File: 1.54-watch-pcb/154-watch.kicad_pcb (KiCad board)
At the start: 4 copper layers, 50.3 x 33 mm, 59 parts, among them J1 CONN_AFC24-S24FIC-00_JUS, J2 Conn_01x06_Female, J3 USB_C_Programming, J4 Jack-DC, J5 Conn_01x02_Male, Q1 Si1308, Q2 BC817, Q3 BC817, Q4 Si2301CDS, SW1 RESET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

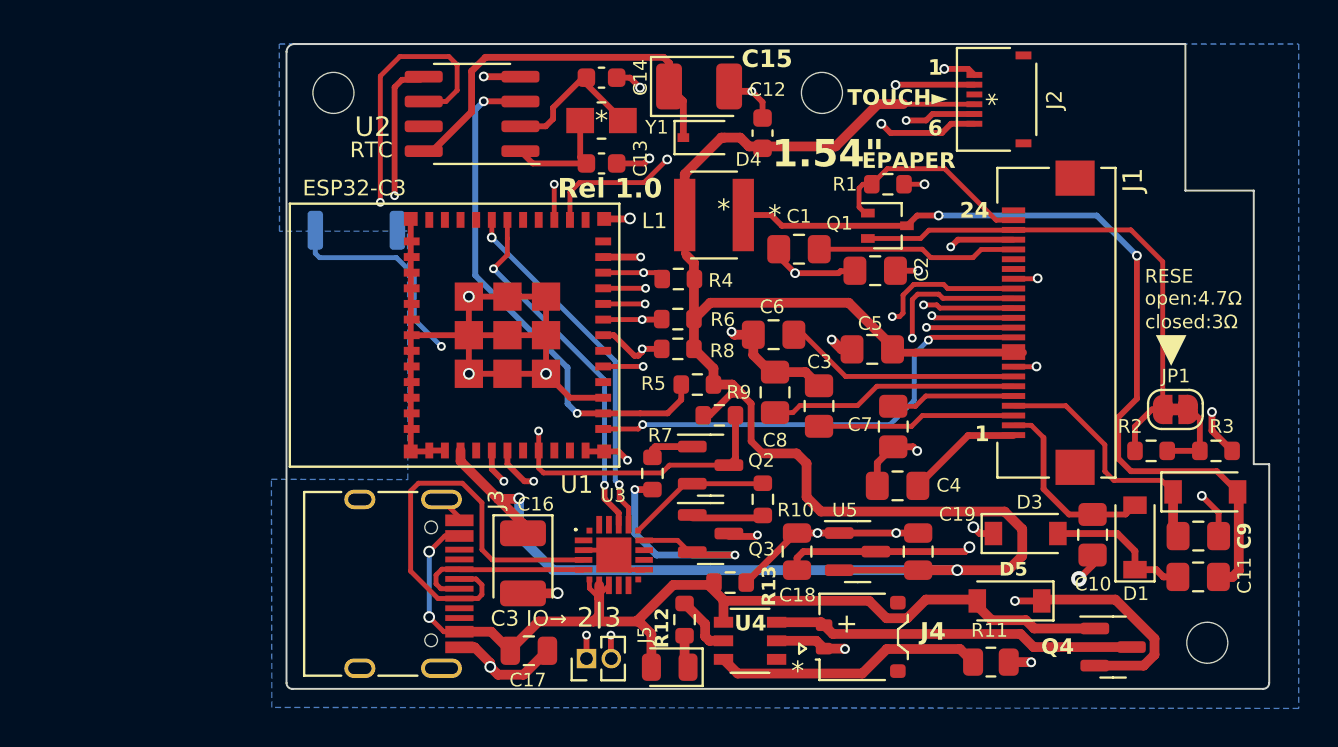
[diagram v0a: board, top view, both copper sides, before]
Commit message: #6 Position well 24 pin FPC
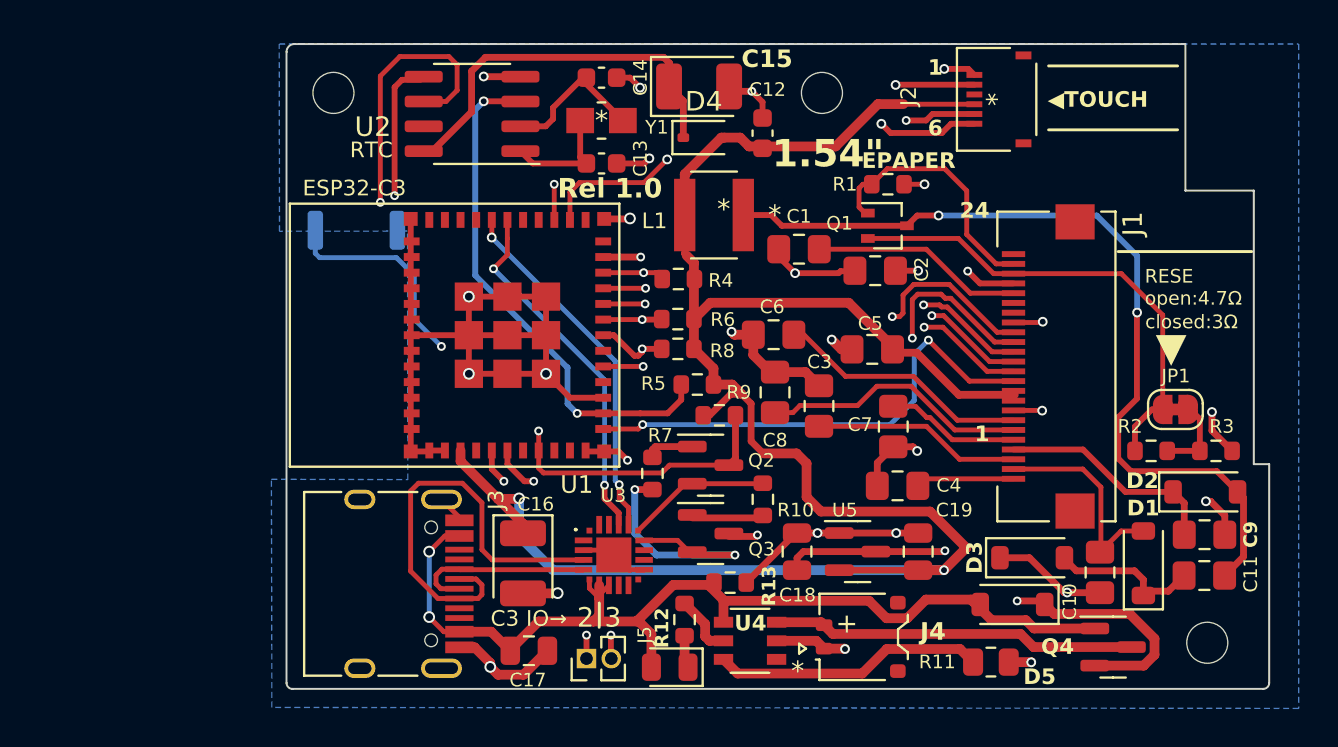
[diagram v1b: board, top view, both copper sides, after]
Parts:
- moved J1 2.24 mm to (111.4, 46.0)
- moved C10 1.96 mm to (113.6, 56.5)
- moved D1 1.39 mm to (115.8, 56.1)
- moved D3 1.28 mm to (110.2, 55.8)
- moved C9 0.33 mm to (119.0, 54.6)
- moved C11 0.33 mm to (119.0, 56.7)
- moved D5 0.23 mm to (109.2, 58.2)
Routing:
- net +3V3: track 112.3 -> 105.6 mm
- net GND: track 103.1 -> 106.7 mm, vias 27 -> 26
- net Net-(Q1-G): track 11.0 -> 13.2 mm
- net Net-(JP1-A): track 26.5 -> 24.6 mm
- net PREVGH: track 13.2 -> 11.5 mm
- net Net-(D1-A): track 9.84 -> 10.9 mm
- net /EPD_CLK: track 21.5 -> 22.4 mm
- net Net-(C8-Pad2): track 12.8 -> 13.7 mm
- net Net-(C6-Pad2): track 12.1 -> 13.1 mm
- net /EPD_RST: track 23.8 -> 24.7 mm
- net /EPD_DC: track 28.0 -> 28.9 mm
- net /EPD_CS: track 28.7 -> 29.7 mm
- net /EPD_BUSY: track 22.9 -> 23.8 mm
- net /VCOM: track 5.96 -> 5.05 mm
- net /EPD_MOSI: track 24.3 -> 25.1 mm
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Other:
- board text added: "◀TOUCH"
- board text removed: "TOUCH►"

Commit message: Add some test points in case UART works incorrectly https://github.com/martinberlin/H-spi-adapters/issues/9
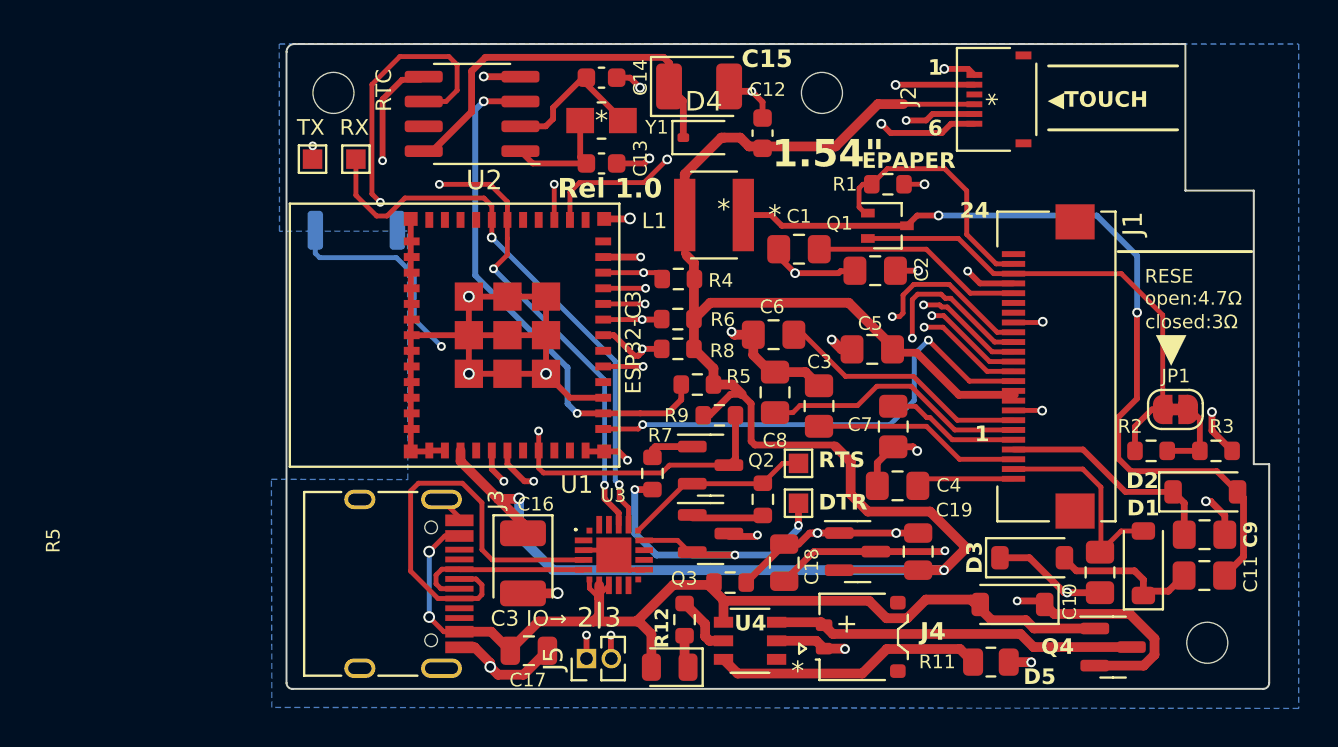
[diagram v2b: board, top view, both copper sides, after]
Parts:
- added TP1: 32Khz, TestPoint:TestPoint_Pad_1.0x1.0mm, F.Cu at (98.2, 51.0)
- added TP2: 32Khz, TestPoint:TestPoint_Pad_1.0x1.0mm, F.Cu at (98.2, 53.0)
- added TP3: 32Khz, TestPoint:TestPoint_Pad_1.0x1.0mm, F.Cu at (73.3, 35.4)
- added TP4: 32Khz, TestPoint:TestPoint_Pad_1.0x1.0mm, F.Cu at (75.5, 35.4)
- J1: value CONN_AFC24-S24FIC-00_JUS -> AFC24-S24FIC-00
- U1: value ESP32-C3-MINI -> ESP32-C3-MINI-1-N4
- U4: value SOT-23-5_TPW -> TP4057-42-SOT26-R
- moved C18 0.87 mm to (97.5, 56.0)
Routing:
- net TX: track 18.6 -> 31.6 mm, vias 2 -> 4
- net RX: track 18.5 -> 29.0 mm
- net /CTS: track 13.7 -> 18.8 mm, vias 2 -> 3
- net BOOTMODE: track 55.4 -> 57.9 mm
- net /RTS: track 7.38 -> 9.65 mm
- net Net-(D5-K): track 25.0 -> 25.6 mm
- net /I2C_SDA: track 49.0 -> 49.5 mm
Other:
- board text added: "DTR"
- board text added: "R5"
- board text added: "RTS"
- board text added: "RX"
- board text added: "TX"

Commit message: 1.54" Rel 1.0 sent to fabrication
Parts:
- moved SW1 0.93 mm to (76.5, 39.0)
- moved D2 0.37 mm to (118.7, 52.3)
- moved C11 0.09 mm to (119.0, 56.8)
- moved C9 0.09 mm to (119.1, 54.6)
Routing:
- net Net-(Q2-C): track 33.7 -> 32.1 mm
- net GND: track 106.9 -> 107.4 mm
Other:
- outline, holes or cut-outs redrawn

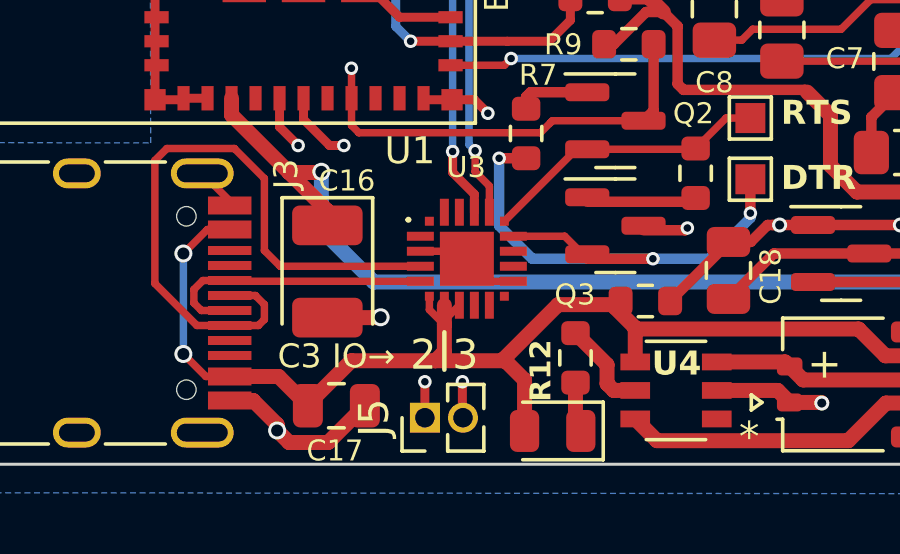
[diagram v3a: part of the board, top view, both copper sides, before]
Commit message: Sharp LCD prod. 1.0 and update to failed watch
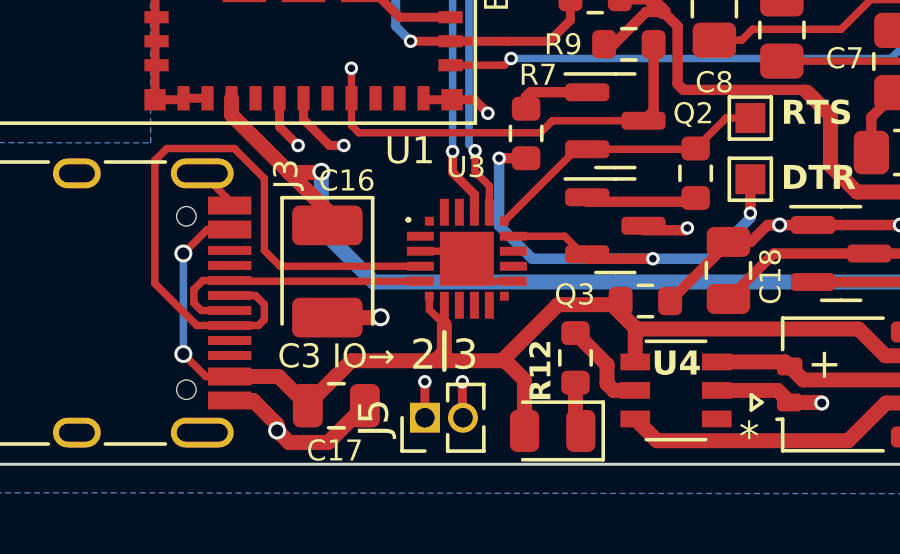
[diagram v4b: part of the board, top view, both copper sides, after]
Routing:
- net VBUS: track 50.9 -> 49.6 mm
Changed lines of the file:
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@@
   (segment (start 89.975 58.995) (end 89.92 59.05) (width 0.5) (layer "F.Cu") (net 3))
   (segment (start 79.3 58.825) (end 80.05 59.575) (width 0.25) (layer "F.Cu") (net 3))
-  (segment (start 88 57.85) (end 88 57.2) (width 0.5) (layer "F.Cu") (net 3))
   (segment (start 80.1 54.675) (end 79.3 55.475) (width 0.25) (layer "F.Cu") (net 3))
   (segment (start 88 58.75) (end 88 57.85) (width 0.5) (layer "F.Cu") (net 3))
@@
   (segment (start 104.721812 57.93) (end 107.03 57.93) (width 0.5) (layer "F.Cu") (net 3))
   (segment (start 87.7 59.05) (end 88 58.75) (width 0.5) (layer "F.Cu") (net 3))
-  (segment (start 88.5 57.2) (end 88 57.7) (width 0.25) (layer "F.Cu") (net 3))
   (segment (start 84.9 59.05) (end 83.45 60.5) (width 0.5) (layer "F.Cu") (net 3))
   (segment (start 82.475 59.575) (end 80.845 59.575) (width 0.5) (layer "F.Cu") (net 3))

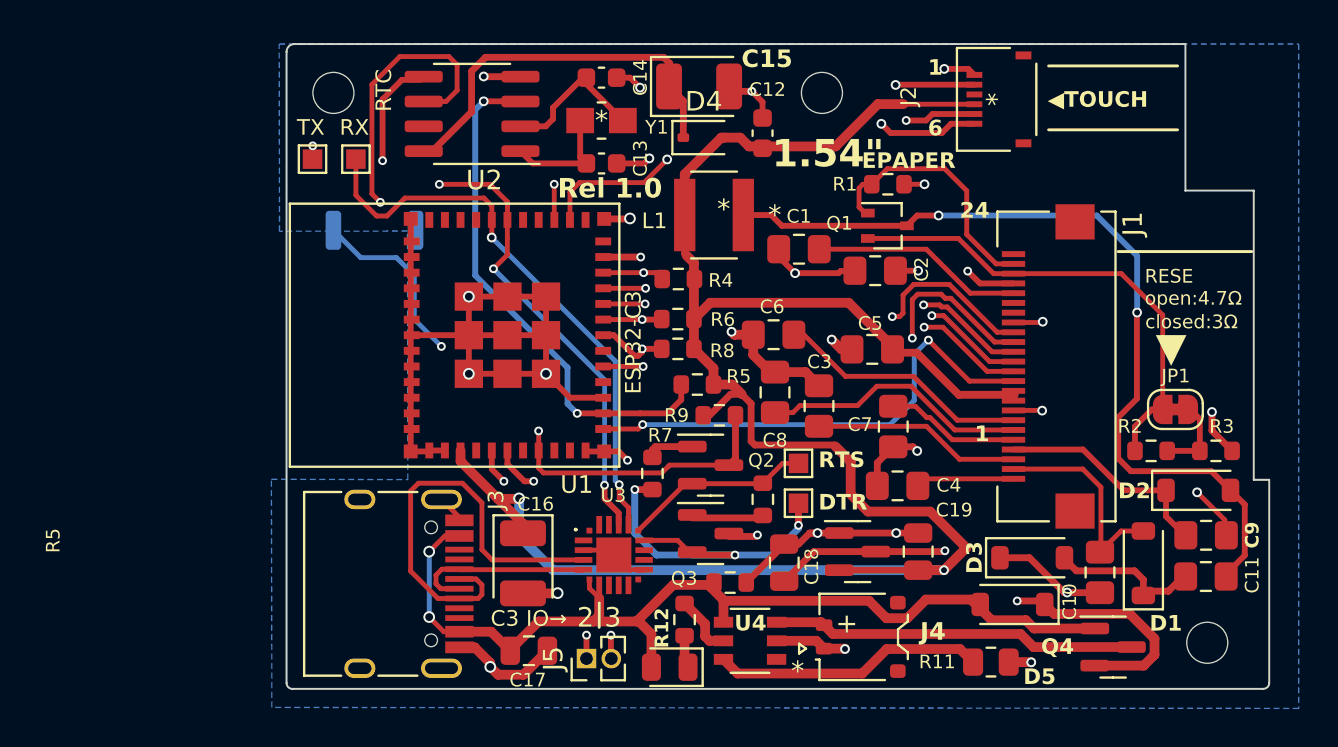
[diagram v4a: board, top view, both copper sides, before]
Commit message: Update UART in 1.54" watch PCB
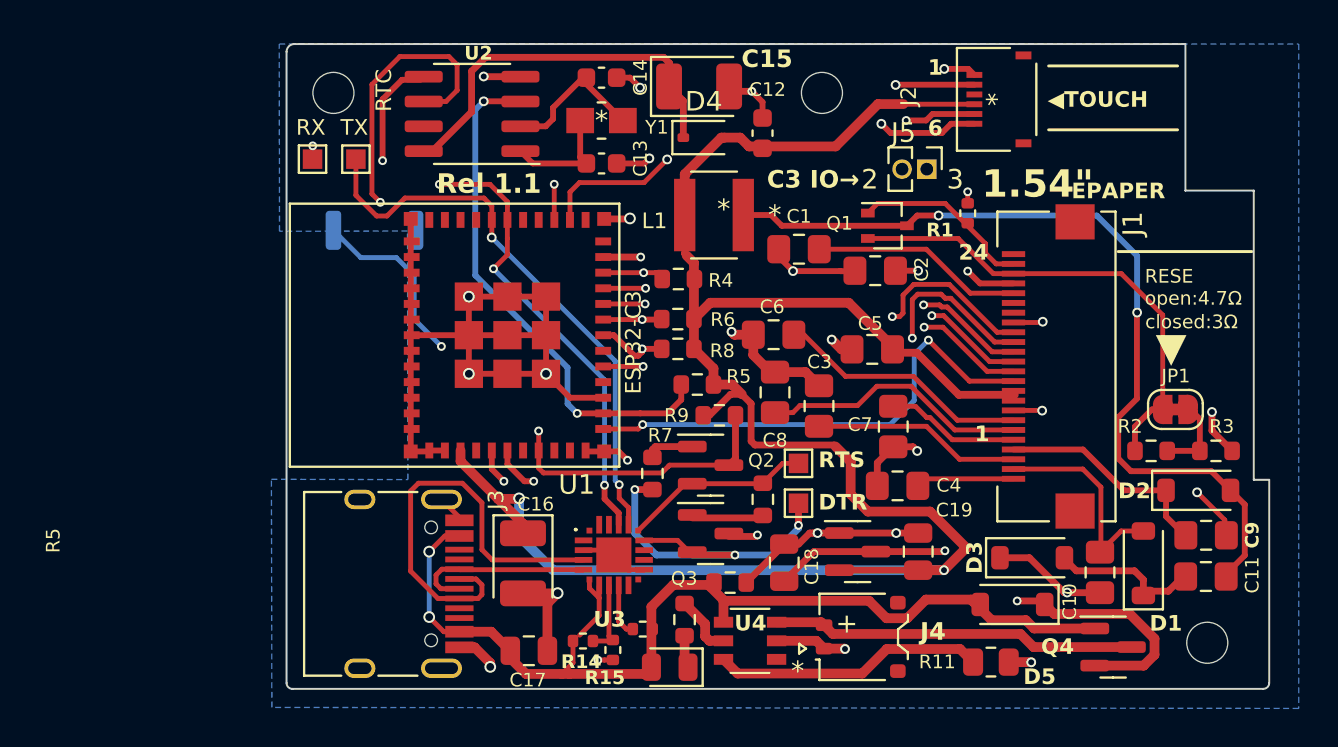
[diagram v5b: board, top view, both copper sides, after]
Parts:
- added R14: 22K, Resistor_SMD:R_0402_1005Metric, F.Cu at (87.2, 60.0)
- added R15: 47K, Resistor_SMD:R_0402_1005Metric, F.Cu at (88.7, 60.5)
- added R16: 10 K, Resistor_SMD:R_0402_1005Metric, F.Cu at (90.2, 59.4)
- R1: footprint Resistor_SMD:R_0603_1608Metric -> Resistor_SMD:R_0402_1005Metric
- moved J5 30.5 mm to (104.8, 35.9), turned to -90 degrees
- moved R1 4.35 mm to (106.9, 38.2), turned to 90 degrees
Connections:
- U3 pad 8: VBUS -> Net-(U3-VBUS)
- U3 pad 9: unconnected-(U3-~{RST}-Pad9) -> Net-(U3-~{RST})
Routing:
- net /IO_2: track 12.7 -> 32.5 mm, vias 2 -> 1
- net /IO_3: track 13.1 -> 28.2 mm, vias 2 -> 1
- net Net-(Q1-G): track 13.2 -> 9.22 mm
- net Net-(U3-VBUS): track 0.00 -> 3.85 mm
- net VBUS: track 49.6 -> 52.9 mm
- net Net-(U3-~{RST}): track 0.00 -> 2.73 mm
- net GND: track 107.4 -> 107.2 mm, vias 26 -> 27
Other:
- board text added: "Rel 1.1"
- board text removed: "Rel 1.0"

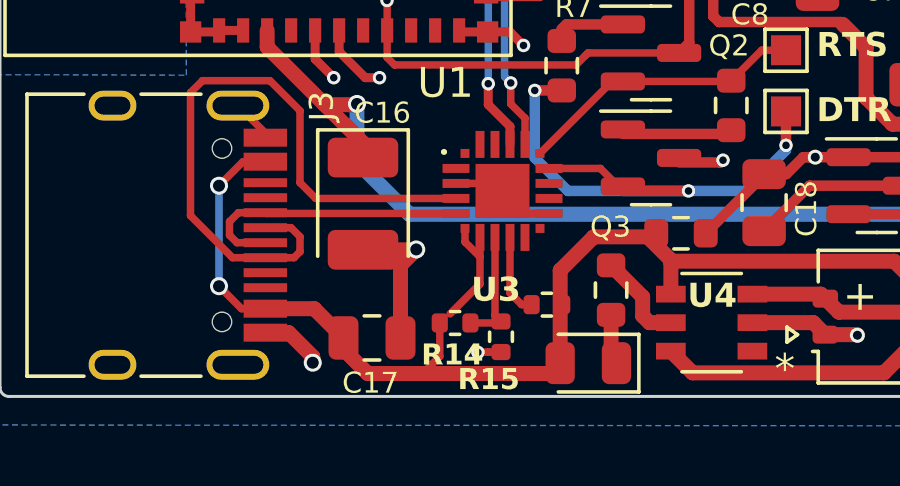
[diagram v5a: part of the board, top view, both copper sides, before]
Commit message: VregIN is the only power input CP2102
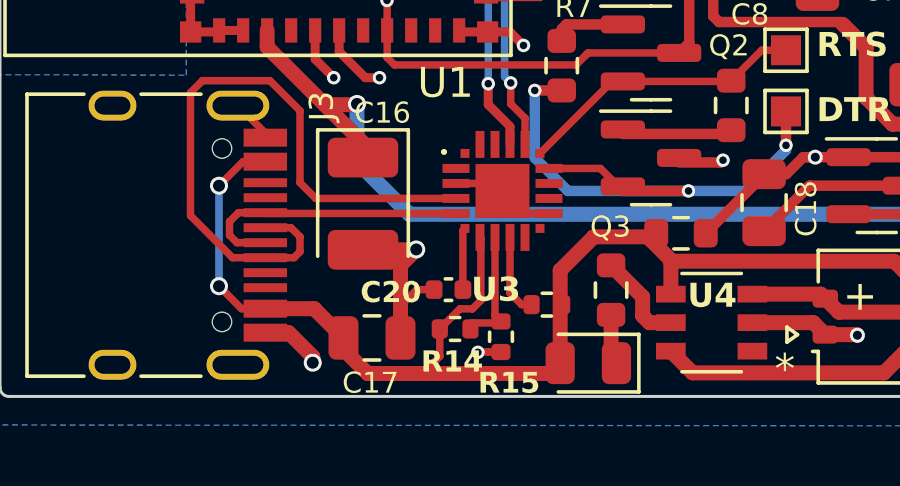
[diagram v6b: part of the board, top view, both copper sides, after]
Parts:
- added C20: 1uF, Capacitor_SMD:C_0402_1005Metric, F.Cu at (87.0, 58.9)
- moved R14 0.20 mm to (87.2, 60.2)
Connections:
- U3 pad 6: VBUS -> Net-(U3-VDD)
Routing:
- net Net-(U3-VDD): track 0.00 -> 2.07 mm
- net GND: track 107.2 -> 108.6 mm
